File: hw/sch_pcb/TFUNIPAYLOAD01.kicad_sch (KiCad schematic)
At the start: 78 parts, among them J1 SM06B-GHS-TB, J2 SM08B-GHS-TB, J3 HEADER_2x03, J4 SM04B-GHS-TB, J5 HEADER_2x15, J6 SM07B-GHS-TB, M1 HOLE, M2 HOLE, M3 HOLE, M4 HOLE, Q1 BC817-25, Q2 BC817-25, SW1 SKRTLAE010, SW2 SKRTLAE010, U1 TPS631000DRLR, U2 ATMEGA1284P-AU, U3 TPS631000DRLR, Y1 8 MHz

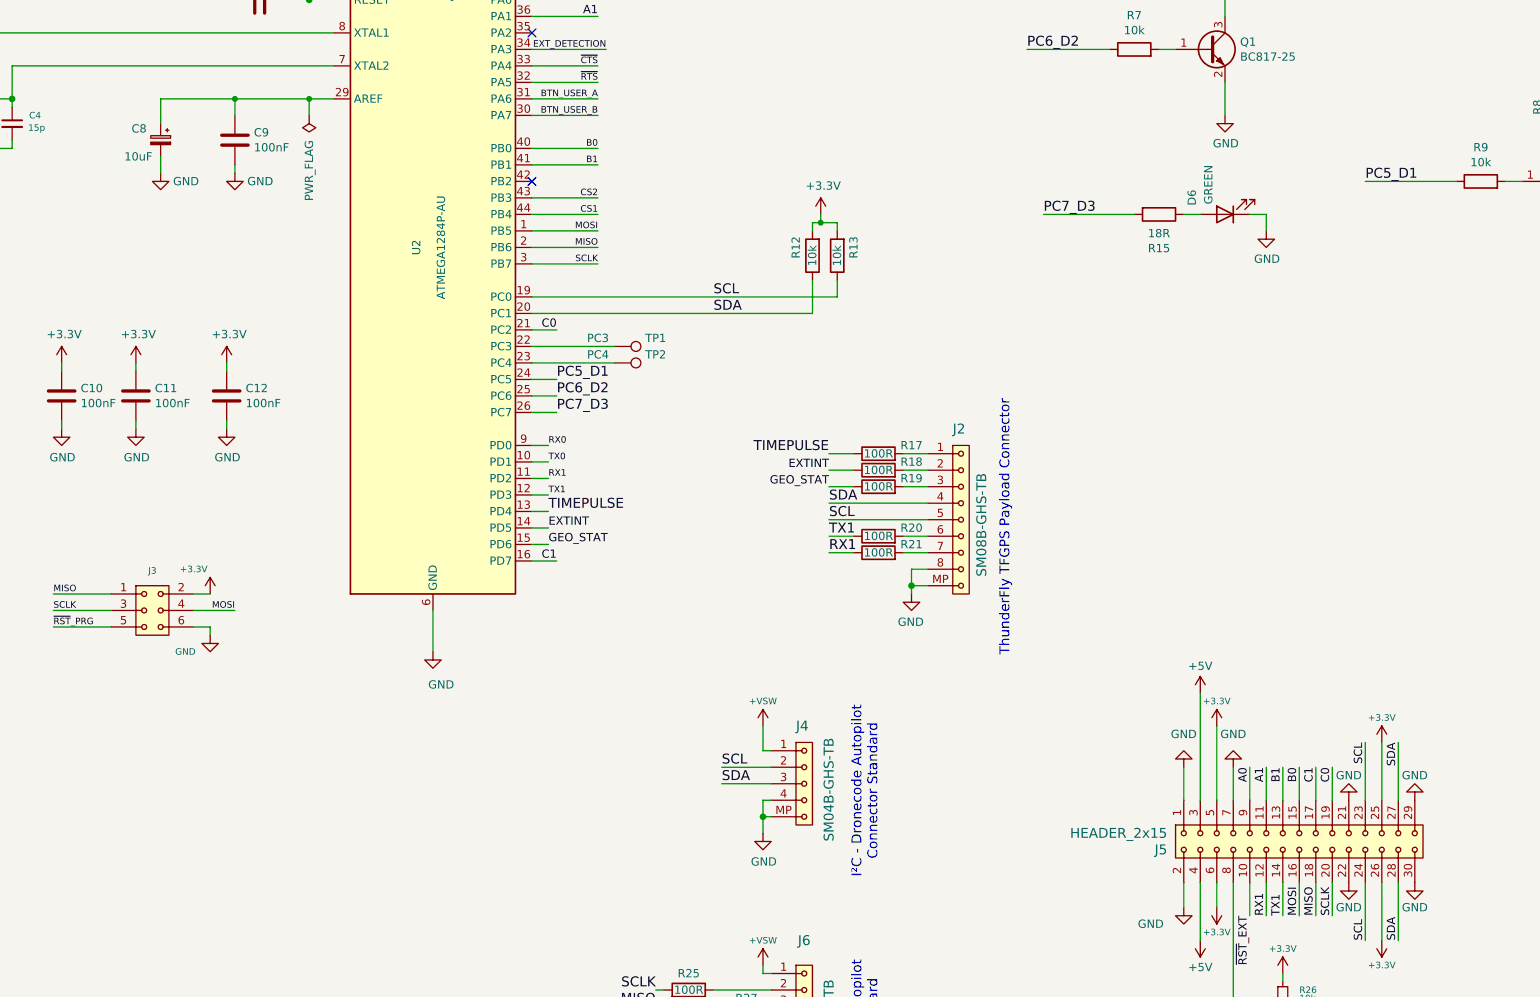
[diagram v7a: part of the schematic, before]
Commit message: Pinheader changed to footprint with square pads. Routing more nets.
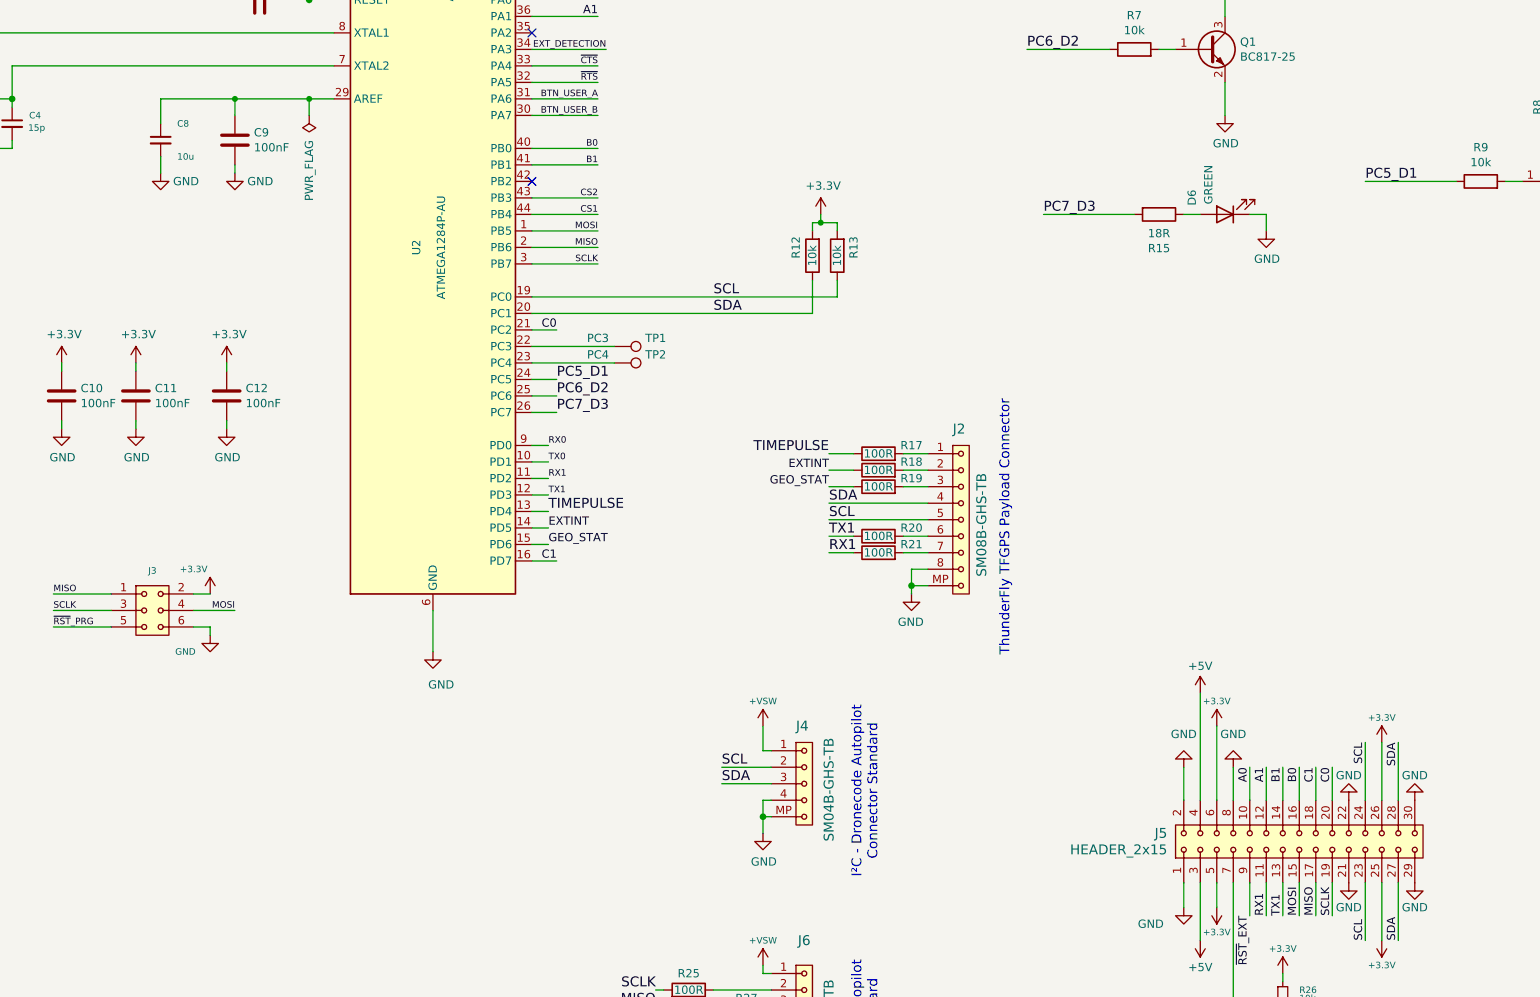
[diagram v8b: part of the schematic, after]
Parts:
- removed C8: 10uF, Capacitor_Tantalum_SMD:CP_EIA-3216-18_Kemet-A, symbol Device:C_Polarized_Small
- added C8: 10u, Capacitor_SMD:C_0805_2012Metric, symbol Device:C_Small
- R25, R27, R28, R29, R30: footprint Resistor_SMD:R_0603_1608Metric -> Resistor_SMD:R_0805_2012Metric
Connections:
- net A0: now also J5.10; no longer J5.9
- net A1: now also J5.12; no longer J5.11
- net B0: now also J5.16; no longer J5.15
- net B1: now also J5.14; no longer J5.13
- net C0: now also J5.20; no longer J5.19
- net C1: now also J5.18; no longer J5.17
- net EXT_DETECTION: now also J5.7; no longer J5.8
- net GND: now also J5.8, C8.2; no longer J5.7
- net MISO: now also J5.17; no longer J5.18
- net MOSI: now also J5.15; no longer J5.16
- net RX1: now also J5.11; no longer J5.12
- net SCLK: now also J5.19; no longer J5.20
- net TX1: now also J5.13; no longer J5.14
- net ~{RST}_EXT: now also J5.9; no longer J5.10
- net at C9.1, U2.29 (AREF): now also C8.1
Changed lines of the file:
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@@
 			)
 		)
-		(property "Footprint" "Resistor_SMD:R_0603_1608Metric"
+		(property "Footprint" "Resistor_SMD:R_0805_2012Metric"
 			(at 251.46 229.108 90)
 			(effects
@@
 	)
 	(symbol
-		(lib_id "Device:C_Polarized_Small")
-		(at 172.72 86.36 0)
-		(mirror y)
-		(unit 1)
-		(exclude_from_sim yes)
-		(in_bom yes)
-		(on_board yes)
-		(dnp no)
-		(property "Reference" "C8"
-			(at 170.561 84.6018 0)
-			(effects
-				(font
-					(size 1.27 1.27)
-				)
-				(justify left)
-			)
-		)
-		(property "Value" "10uF"
-			(at 171.45 88.9 0)
-			(effects
-				(font
-					(size 1.27 1.27)
-				)
-				(justify left)
-			)
-		)
-		(property "Footprint" "Capacitor_Tantalum_SMD:CP_EIA-3216-18_Kemet-A"
-			(at 172.72 86.36 0)
-			(effects
-				(font
-					(size 1.27 1.27)
-				)
-				(hide yes)
-			)
-		)
-		(property "Datasheet" "https://eu.mouser.com/datasheet/2/40/TAJ-3165264.pdf"
-			(at 172.72 86.36 0)
-			(effects
-				(font
-					(size 1.27 1.27)
-				)
-				(hide yes)
-			)
-		)
-		(property "Description" ""
-			(at 172.72 86.36 0)
-			(effects
-				(font
-					(size 1.27 1.27)
-				)
-				(hide yes)
-			)
-		)
-		(property "UST_ID" "65089dd0462c6d9e720542b3"
-			(at 172.72 86.36 0)
-			(effects
-				(font
-					(size 1.27 1.27)
-				)
-				(hide yes)
-			)
-		)
-		(pin "1"
-		)
-		(pin "2"
-		)
-		(instances
-			(project "TFUNIPAYLOAD01"
-				(path "/0a87ced0-2af2-43c5-a56c-218f7013d76f"
-					(reference "C8")
-					(unit 1)
-				)
-			)
-		)
-	)
-	(symbol
 		(lib_id "Device:C_Small")
 		(at 149.86 83.82 0)
@@
 			)
 		)
-		(property "Footprint" "Resistor_SMD:R_0603_1608Metric"
+		(property "Footprint" "Resistor_SMD:R_0805_2012Metric"
 			(at 259.08 221.488 90)
 			(effects
@@
 			)
 		)
-		(property "Footprint" "Resistor_SMD:R_0603_1608Metric"
+		(property "Footprint" "Resistor_SMD:R_0805_2012Metric"
 			(at 260.35 226.568 90)
 			(effects
@@
 	)
 	(symbol
+		(lib_id "Device:C_Small")
+		(at 172.72 86.36 0)
+		(unit 1)
+		(exclude_from_sim no)
+		(in_bom yes)
+		(on_board yes)
+		(dnp no)
+		(property "Reference" "C8"
+			(at 175.26 83.82 0)
+			(effects
+				(font
+					(size 1 1)
+				)
+				(justify left)
+			)
+		)
+		(property "Value" "10u"
+			(at 175.26 88.9 0)
+			(effects
+				(font
+					(size 1 1)
+				)
+				(justify left)
+			)
+		)
+		(property "Footprint" "Capacitor_SMD:C_0805_2012Metric"
+			(at 172.72 86.36 0)
+			(effects
+				(font
+					(size 1 1)
+				)
+				(hide yes)
+			)
+		)
+		(property "Datasheet" "~"
+			(at 172.72 86.36 0)
+			(effects
+				(font
+					(size 1 1)
+				)
+				(hide yes)
+			)
+		)
+		(property "Description" ""
+			(at 172.72 86.36 0)
+			(effects
+				(font
+					(size 1.27 1.27)
+				)
+				(hide yes)
+			)
+		)
+		(property "UST_ID" "5c70984712875079b91f8b53"
+			(at 172.72 86.36 0)
+			(effects
+				(font
+					(size 1 1)
+				)
+				(hide yes)
+			)
+		)
+		(pin "1"
+		)
+		(pin "2"
+		)
+		(instances
+			(project "TFUNIPAYLOAD01"
+				(path "/0a87ced0-2af2-43c5-a56c-218f7013d76f"
+					(reference "C8")
+					(unit 1)
+				)
+			)
+		)
+	)
+	(symbol
 		(lib_id "power:+VSW")
 		(at 265.43 213.36 0)
@@
 			)
 		)
-		(property "Footprint" "Resistor_SMD:R_0603_1608Metric"
+		(property "Footprint" "Resistor_SMD:R_0805_2012Metric"
 			(at 254 224.028 90)
 			(effects
@@
 			)
 		)
-		(property "Footprint" "Resistor_SMD:R_0603_1608Metric"
+		(property "Footprint" "Resistor_SMD:R_0805_2012Metric"
 			(at 254 218.948 90)
 			(effects
@@
 		(lib_id "MLAB_HEADER:HEADER_2x15")
 		(at 347.98 194.31 90)
-		(mirror x)
 		(unit 1)
 		(exclude_from_sim no)
@@
 		(dnp no)
 		(property "Reference" "J5"
-			(at 327.66 195.58 90)
+			(at 327.66 193.04 90)
 			(effects
 				(font
@@
 		)
 		(property "Value" "HEADER_2x15"
-			(at 327.66 193.04 90)
+			(at 327.66 195.58 90)
 			(effects
 				(font
